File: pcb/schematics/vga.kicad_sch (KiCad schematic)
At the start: 23 parts

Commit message: add global symbals to the video controller
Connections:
- net HSYNC renamed VGA_HSYNC
- net VSYNC renamed VGA_VSYNC
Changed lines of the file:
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@@
     )
   )
-  (global_label "HSYNC" (shape input) (at 210.82 81.28 0) (fields_autoplaced)
+  (global_label "VGA_HSYNC" (shape input) (at 210.82 81.28 0) (fields_autoplaced)
     (effects (font (size 1.27 1.27)) (justify left))
-    (property "Intersheetrefs" "${INTERSHEET_REFS}" (id 0) (at 219.8912 81.28 0)
+    (property "Intersheetrefs" "${INTERSHEET_REFS}" (id 0) (at 224.306 81.28 0)
       (effects (font (size 1.27 1.27)) (justify left))
     )
@@
     )
   )
-  (global_label "VSYNC" (shape input) (at 210.82 86.36 0) (fields_autoplaced)
+  (global_label "VGA_VSYNC" (shape input) (at 210.82 86.36 0) (fields_autoplaced)
     (effects (font (size 1.27 1.27)) (justify left))
-    (property "Intersheetrefs" "${INTERSHEET_REFS}" (id 0) (at 219.6493 86.36 0)
+    (property "Intersheetrefs" "${INTERSHEET_REFS}" (id 0) (at 224.0641 86.36 0)
       (effects (font (size 1.27 1.27)) (justify left))
     )

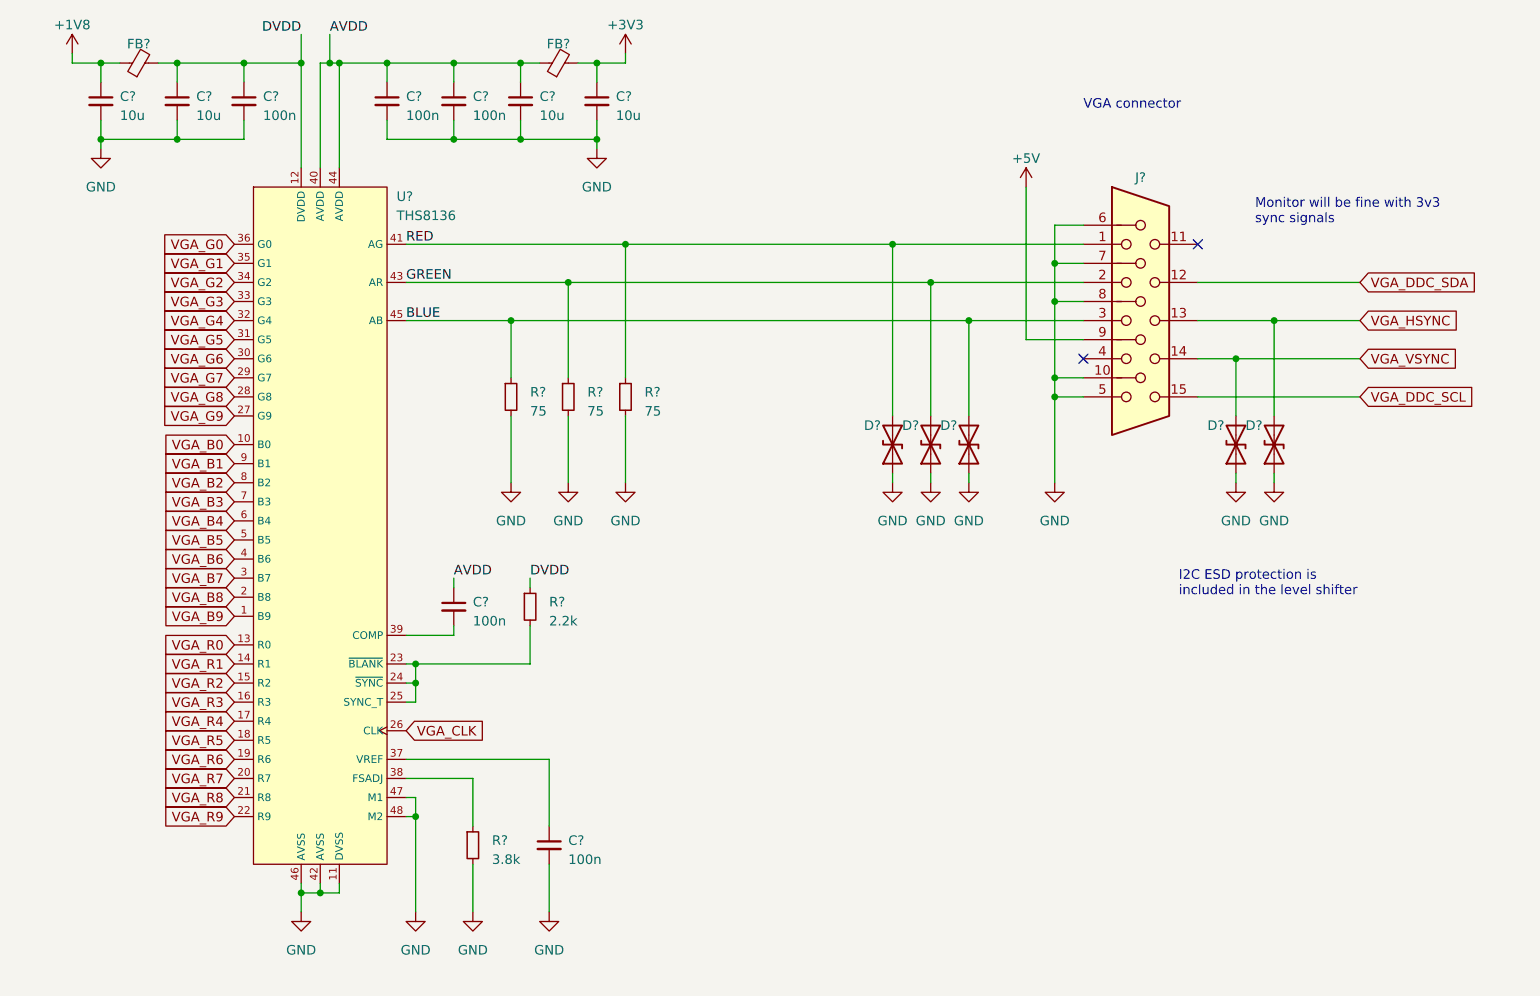
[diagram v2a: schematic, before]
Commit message: choose components and add footprints
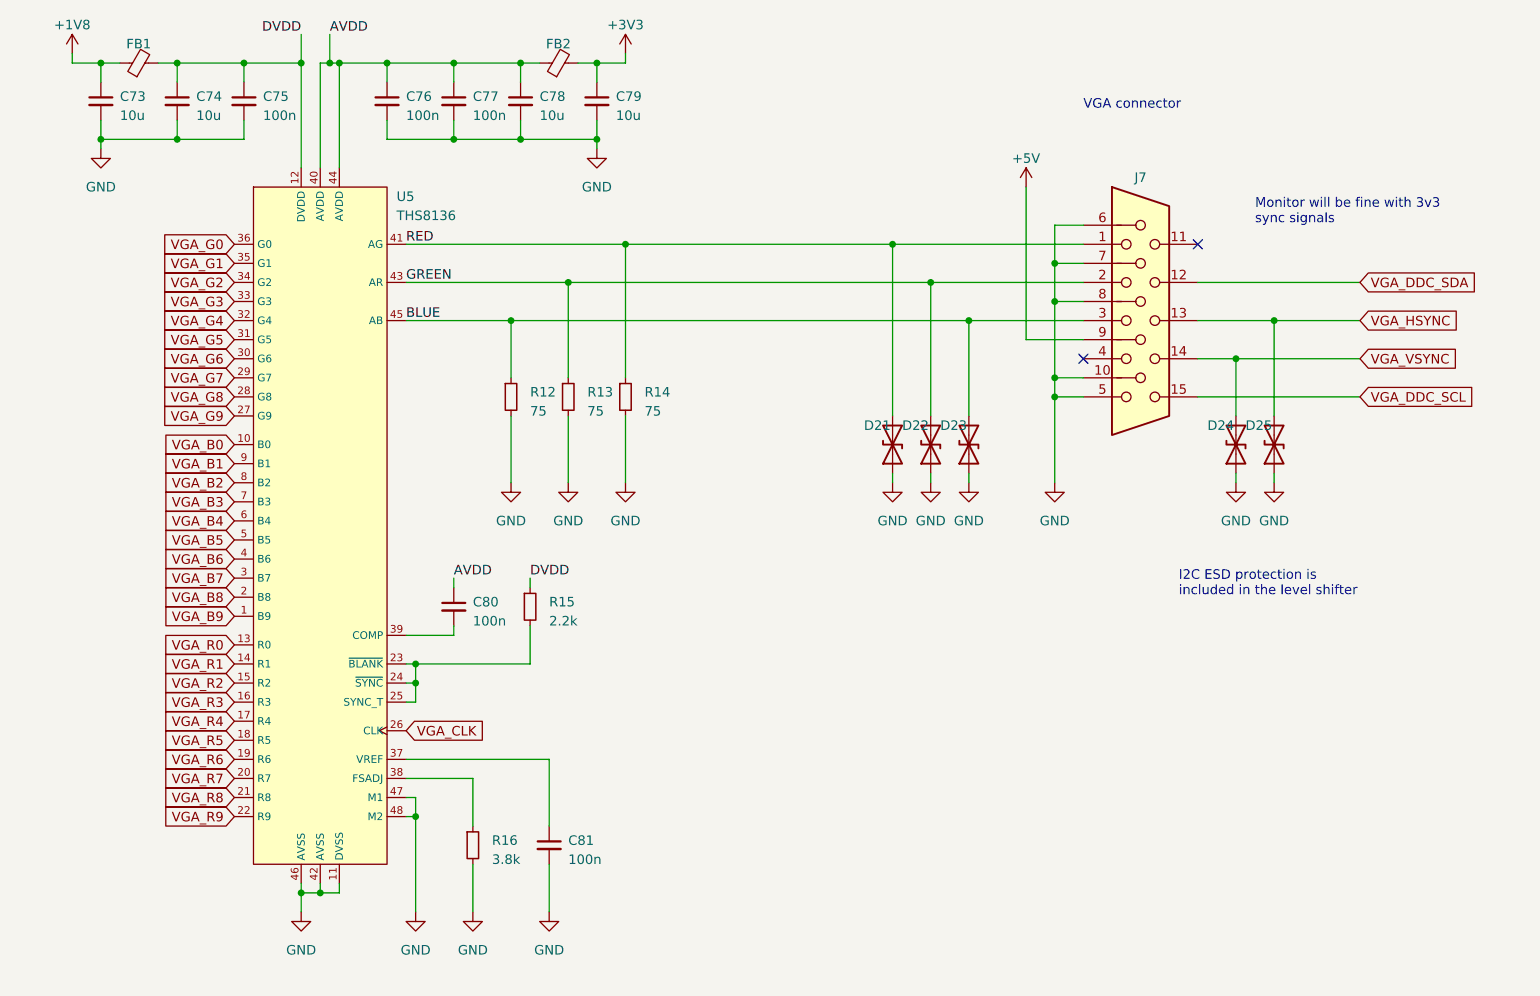
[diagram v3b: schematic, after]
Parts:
- C73, C74, C78, C79: renamed from C?; footprint (none) -> Capacitor_SMD:C_0805_2012Metric; Part Number (none) -> JMK212ABJ106MG-T
- C75, C76, C77, C80, C81: renamed from C?; footprint (none) -> Capacitor_SMD:C_0603_1608Metric; Part Number (none) -> EMK107B7104KA-T
- D21, D22, D23, D24, D25: renamed from D?; footprint (none) -> Diode_SMD:D_0603_1608Metric; Part Number (none) -> 82356240030
- FB1, FB2: renamed from FB?; footprint (none) -> Inductor_SMD:L_0805_2012Metric; Part Number (none) -> MFBM1V2012-150-R
- J7: renamed from J?; footprint (none) -> L77HDE15SD1CH4FVGA:L77HDE15SD1CH4FVGA; Part Number (none) -> L77HDE15SD1CH4FVGA
- R12, R13, R14: renamed from R?; footprint (none) -> Resistor_SMD:R_0603_1608Metric; Part Number (none) -> WR06X75R0FTL
- R15: renamed from R?; footprint (none) -> Resistor_SMD:R_0603_1608Metric; Part Number (none) -> CR0603-JW-222ELF
- R16: renamed from R?; footprint (none) -> Resistor_SMD:R_0603_1608Metric; Part Number (none) -> AC0603FR-073K83L
- U5: renamed from U?; footprint (none) -> Package_QFP:TQFP-48-1EP_7x7mm_P0.5mm_EP5x5mm_ThermalVias; Part Number (none) -> THS8136IPHP

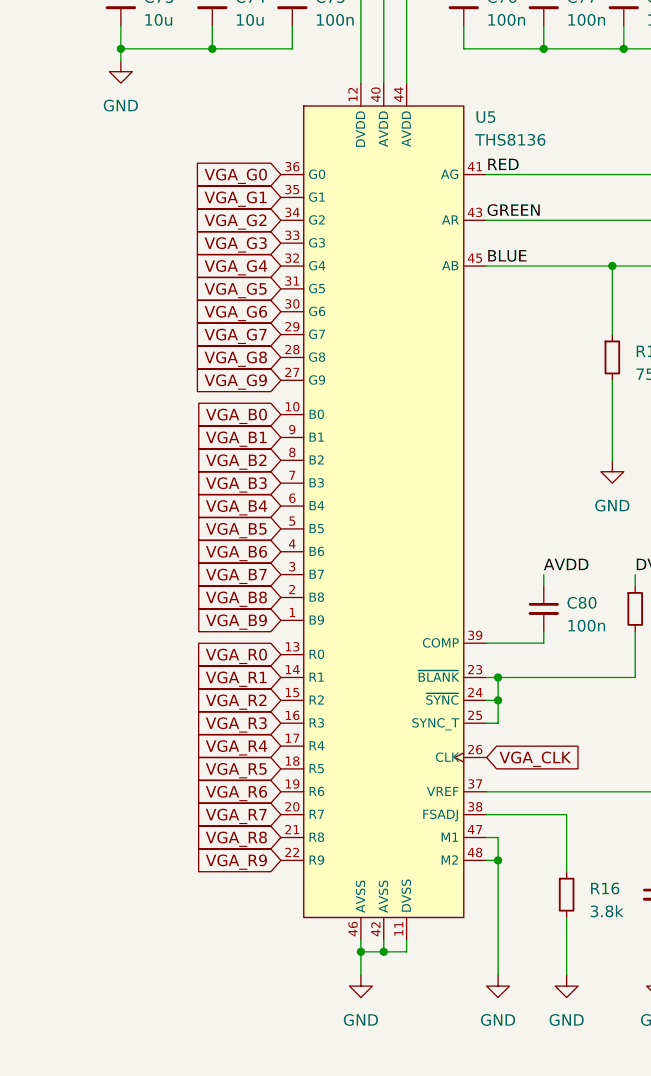
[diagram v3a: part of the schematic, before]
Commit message: change the bank for the hdmi interface
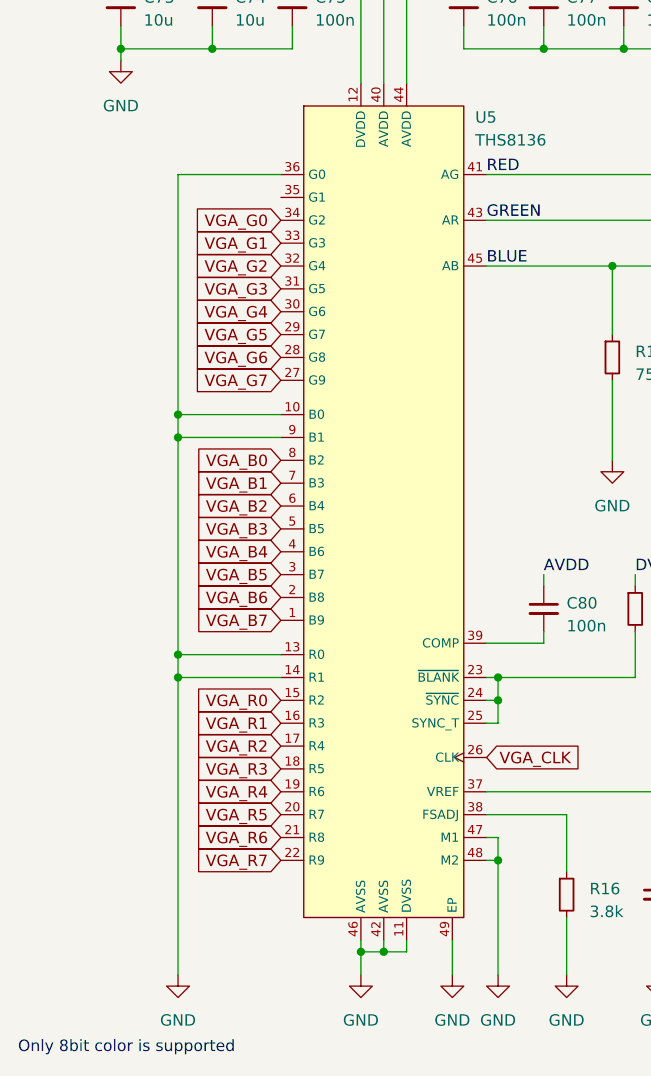
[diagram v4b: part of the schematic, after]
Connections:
- net VGA_B8 is gone; now on net VGA_B6: U5.2 (B8)
- net VGA_B9 is gone; now on net VGA_B7: U5.1 (B9)
- net VGA_G8 is gone; now on net VGA_G6: U5.28 (G8)
- net VGA_G9 is gone; now on net VGA_G7: U5.27 (G9)
- net VGA_R8 is gone; now on net VGA_R6: U5.21 (R8)
- net VGA_R9 is gone; now on net VGA_R7: U5.22 (R9)
- net GND: now also U5.10 (B0), U5.13 (R0), U5.14 (R1), U5.36 (G0), U5.49 (EP), U5.9 (B1)
- net VGA_B0: now also U5.8 (B2); no longer U5.10 (B0)
- net VGA_B1: now also U5.7 (B3); no longer U5.9 (B1)
- net VGA_B2: now also U5.6 (B4); no longer U5.8 (B2)
- net VGA_B3: now also U5.5 (B5); no longer U5.7 (B3)
- net VGA_B4: now also U5.4 (B6); no longer U5.6 (B4)
- net VGA_B5: now also U5.3 (B7); no longer U5.5 (B5)
- net VGA_B6: no longer U5.4 (B6)
- net VGA_B7: no longer U5.3 (B7)
- net VGA_G0: now also U5.34 (G2); no longer U5.36 (G0)
- net VGA_G1: now also U5.33 (G3); no longer U5.35 (G1)
- net VGA_G2: now also U5.32 (G4); no longer U5.34 (G2)
- net VGA_G3: now also U5.31 (G5); no longer U5.33 (G3)
- net VGA_G4: now also U5.30 (G6); no longer U5.32 (G4)
- net VGA_G5: now also U5.29 (G7); no longer U5.31 (G5)
- net VGA_G6: no longer U5.30 (G6)
- net VGA_G7: no longer U5.29 (G7)
- net VGA_R0: now also U5.15 (R2); no longer U5.13 (R0)
- net VGA_R1: now also U5.16 (R3); no longer U5.14 (R1)
- net VGA_R2: now also U5.17 (R4); no longer U5.15 (R2)
- net VGA_R3: now also U5.18 (R5); no longer U5.16 (R3)
- net VGA_R4: now also U5.19 (R6); no longer U5.17 (R4)
- net VGA_R5: now also U5.20 (R7); no longer U5.18 (R5)
- net VGA_R6: no longer U5.19 (R6)
- net VGA_R7: no longer U5.20 (R7)
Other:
- note added: "Only 8bit color is supported"

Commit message: add shield
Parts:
- U: renamed from C78; value 10u -> (none); footprint Capacitor_SMD:C_0805_2012Metric -> (none)
- U: renamed from D24; value D_TVS -> (none); footprint Diode_SMD:D_0603_1608Metric -> (none)
- U: renamed from C77; value 100n -> (none); footprint Capacitor_SMD:C_0603_1608Metric -> (none)
- U: renamed from FB1; value FerriteBead_Small -> (none); footprint Inductor_SMD:L_0805_2012Metric -> (none)
- U: renamed from FB2; value FerriteBead_Small -> (none); footprint Inductor_SMD:L_0805_2012Metric -> (none)
- U: renamed from C75; value 100n -> (none); footprint Capacitor_SMD:C_0603_1608Metric -> (none)
- U: renamed from C79; value 10u -> (none); footprint Capacitor_SMD:C_0805_2012Metric -> (none)
- U: renamed from D23; value D_TVS -> (none); footprint Diode_SMD:D_0603_1608Metric -> (none)
- U: renamed from R14; value 75 -> (none); footprint Resistor_SMD:R_0603_1608Metric -> (none)
- U: renamed from R12; value 75 -> (none); footprint Resistor_SMD:R_0603_1608Metric -> (none)
- U: renamed from C74; value 10u -> (none); footprint Capacitor_SMD:C_0805_2012Metric -> (none)
- U: renamed from R15; value 2.2k -> (none); footprint Resistor_SMD:R_0603_1608Metric -> (none)
- U: renamed from D21; value D_TVS -> (none); footprint Diode_SMD:D_0603_1608Metric -> (none)
- U: renamed from C73; value 10u -> (none); footprint Capacitor_SMD:C_0805_2012Metric -> (none)
- U: renamed from U5; value THS8136 -> (none); footprint Package_QFP:TQFP-48-1EP_7x7mm_P0.5mm_EP5x5mm_ThermalVias -> (none)
- U: renamed from D22; value D_TVS -> (none); footprint Diode_SMD:D_0603_1608Metric -> (none)
- U: renamed from R16; value 3.8k -> (none); footprint Resistor_SMD:R_0603_1608Metric -> (none)
- U: renamed from C76; value 100n -> (none); footprint Capacitor_SMD:C_0603_1608Metric -> (none)
- U: renamed from R13; value 75 -> (none); footprint Resistor_SMD:R_0603_1608Metric -> (none)
- U: renamed from C81; value 100n -> (none); footprint Capacitor_SMD:C_0603_1608Metric -> (none)
- U: renamed from D25; value D_TVS -> (none); footprint Diode_SMD:D_0603_1608Metric -> (none)
- U: renamed from C80; value 100n -> (none); footprint Capacitor_SMD:C_0603_1608Metric -> (none)
- U: renamed from J7; value DB15_Female_HighDensity -> (none); footprint L77HDE15SD1CH4FVGA:L77HDE15SD1CH4FVGA -> (none)

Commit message: passed erc and drc
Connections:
- net GND: now also U.35 (G1)
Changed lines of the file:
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@@
   (junction (at 62.23 46.99) (diameter 0) (color 0 0 0 0)
   )
+  (junction (at 73.66 44.45) (diameter 0) (color 0 0 0 0)
+  )
   (junction (at 43.18 57.15) (diameter 0) (color 0 0 0 0)
   )
@@
   (junction (at 85.09 147.32) (diameter 0) (color 0 0 0 0)
   )
+  (junction (at 49.53 73.66) (diameter 0) (color 0 0 0 0)
+  )
   (junction (at 49.53 100.33) (diameter 0) (color 0 0 0 0)
   )
+  (junction (at 69.85 44.45) (diameter 0) (color 0 0 0 0)
+  )
   (junction (at 170.18 88.9) (diameter 0) (color 0 0 0 0)
   )
@@
     (stroke (width 0) (type default))
   )
+  (wire (pts (xy 73.66 44.45) (xy 73.66 46.99))
+    (stroke (width 0) (type default))
+  )
   (wire (pts (xy 199.39 81.28) (xy 210.82 81.28))
     (stroke (width 0) (type default))
@@
     (stroke (width 0) (type default))
   )
-  (wire (pts (xy 73.66 43.18) (xy 73.66 46.99))
+  (wire (pts (xy 73.66 43.18) (xy 73.66 44.45))
     (stroke (width 0) (type default))
   )
@@
     (stroke (width 0) (type default))
   )
+  (wire (pts (xy 49.53 73.66) (xy 49.53 97.79))
+    (stroke (width 0) (type default))
+  )
   (wire (pts (xy 97.79 81.28) (xy 158.75 81.28))
     (stroke (width 0) (type default))
@@
     (stroke (width 0) (type default))
   )
-  (wire (pts (xy 49.53 71.12) (xy 49.53 97.79))
+  (wire (pts (xy 49.53 71.12) (xy 49.53 73.66))
     (stroke (width 0) (type default))
   )
@@
     (stroke (width 0) (type default))
   )
+  (wire (pts (xy 69.85 44.45) (xy 69.85 46.99))
+    (stroke (width 0) (type default))
+  )
   (wire (pts (xy 73.66 46.99) (xy 74.93 46.99))
     (stroke (width 0) (type default))
@@
     (stroke (width 0) (type default))
   )
-  (wire (pts (xy 69.85 43.18) (xy 69.85 46.99))
+  (wire (pts (xy 69.85 43.18) (xy 69.85 44.45))
     (stroke (width 0) (type default))
   )
@@
     (stroke (width 0) (type default))
   )
+  (wire (pts (xy 49.53 73.66) (xy 60.96 73.66))
+    (stroke (width 0) (type default))
+  )
   (wire (pts (xy 83.82 81.28) (xy 97.79 81.28))
     (stroke (width 0) (type default))
@@
     (pin "2")
   )
+  (symbol (lib_id "power:PWR_FLAG") (at 69.85 44.45 90) (unit 1)
+    (in_bom yes) (on_board yes) (fields_autoplaced)
+    (default_instance (reference "#FLG") (unit 1) (value "PWR_FLAG") (footprint ""))
+    (property "Reference" "#FLG" (id 0) (at 67.945 44.45 0)
+      (effects (font (size 1.27 1.27)) hide)
+    )
+    (property "Value" "PWR_FLAG" (id 1) (at 66.04 45.085 90)
+      (effects (font (size 1.27 1.27)) (justify left))
+    )
+    (property "Footprint" "" (id 2) (at 69.85 44.45 0)
+      (effects (font (size 1.27 1.27)) hide)
+    )
+    (property "Datasheet" "~" (id 3) (at 69.85 44.45 0)
+      (effects (font (size 1.27 1.27)) hide)
+    )
+    (pin "1")
+  )
   (symbol (lib_id "power:GND") (at 80.01 160.02 0) (unit 1)
     (in_bom yes) (on_board yes) (fields_autoplaced)
@@
     (pin "2")
   )
+  (symbol (lib_id "power:PWR_FLAG") (at 73.66 44.45 270) (unit 1)
+    (in_bom yes) (on_board yes) (fields_autoplaced)
+    (default_instance (reference "#FLG") (unit 1) (value "PWR_FLAG") (footprint ""))
+    (property "Reference" "#FLG" (id 0) (at 75.565 44.45 0)
+      (effects (font (size 1.27 1.27)) hide)
+    )
+    (property "Value" "PWR_FLAG" (id 1) (at 77.47 45.085 90)
+      (effects (font (size 1.27 1.27)) (justify left))
+    )
+    (property "Footprint" "" (id 2) (at 73.66 44.45 0)
+      (effects (font (size 1.27 1.27)) hide)
+    )
+    (property "Datasheet" "~" (id 3) (at 73.66 44.45 0)
+      (effects (font (size 1.27 1.27)) hide)
+    )
+    (pin "1")
+  )
   (symbol (lib_id "Device:D_TVS") (at 199.39 97.79 90) (unit 1)
